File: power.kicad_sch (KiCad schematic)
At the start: 1 part, among them U1 STM32H753ZIT6

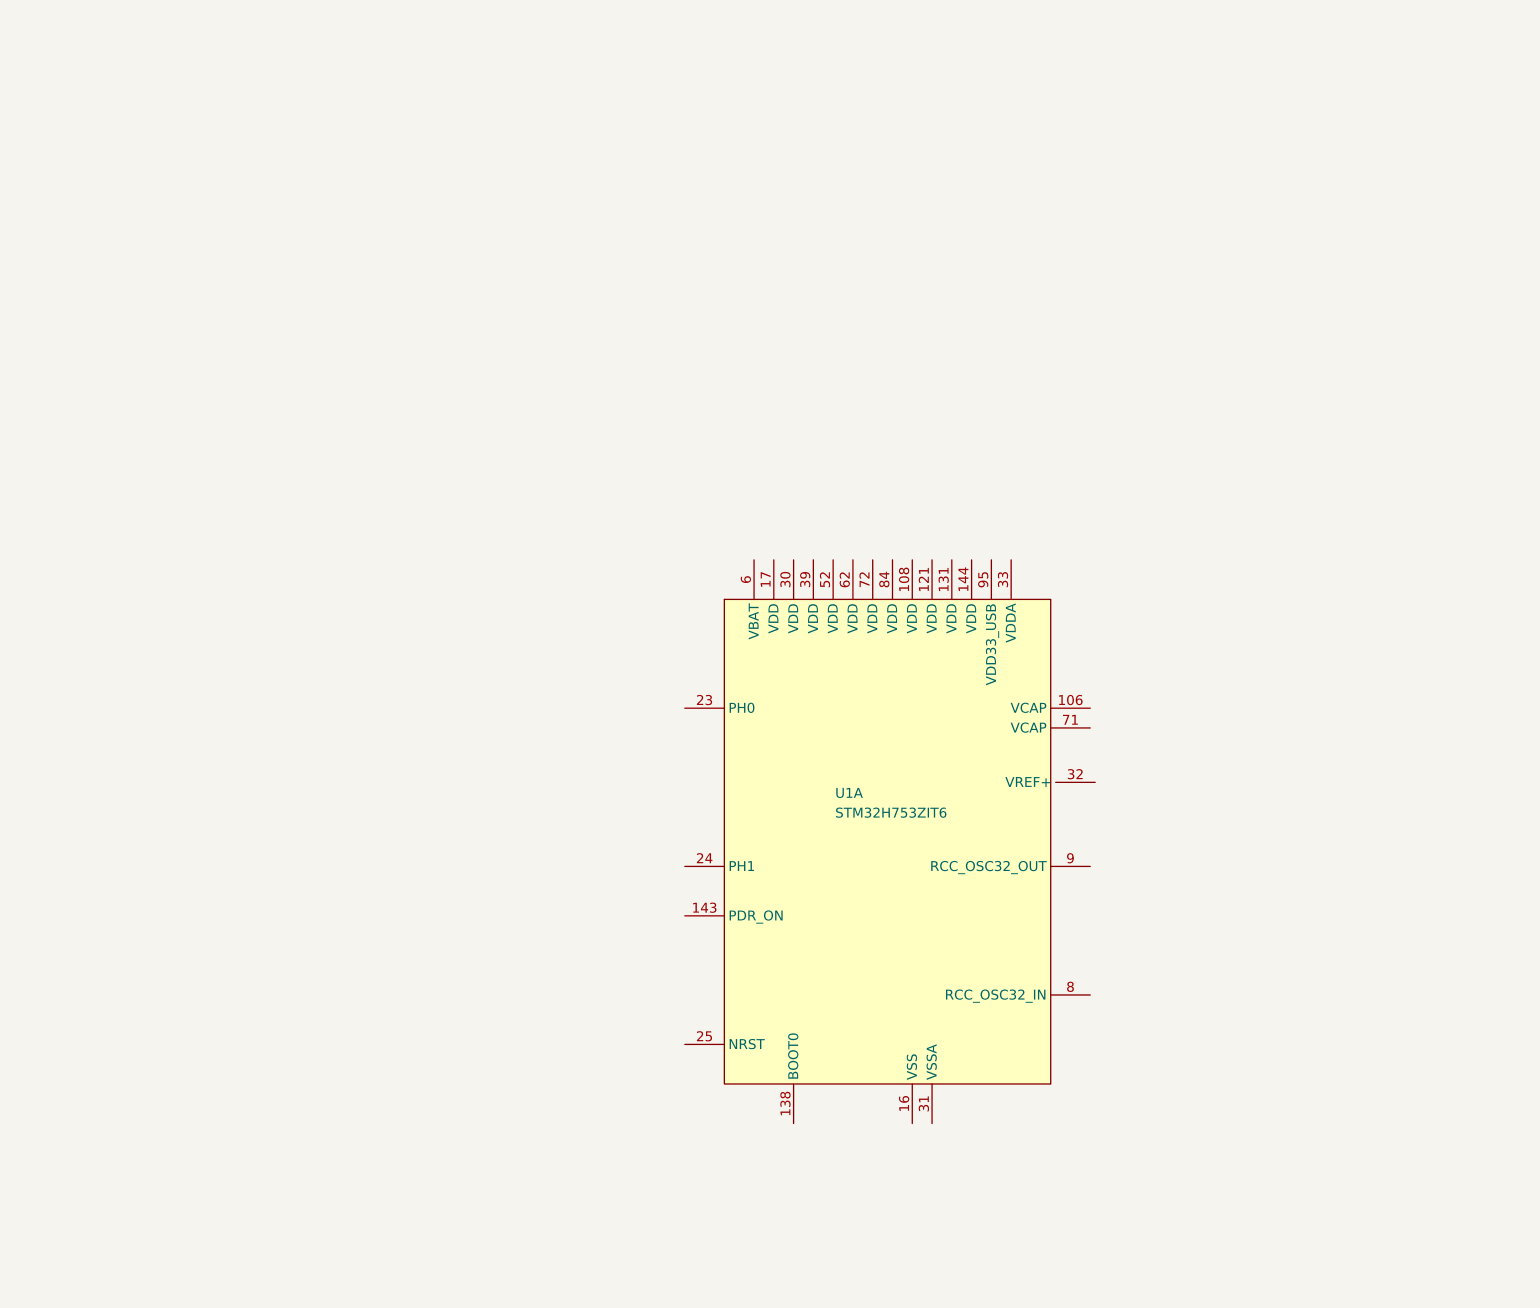
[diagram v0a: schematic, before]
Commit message: add SDIO
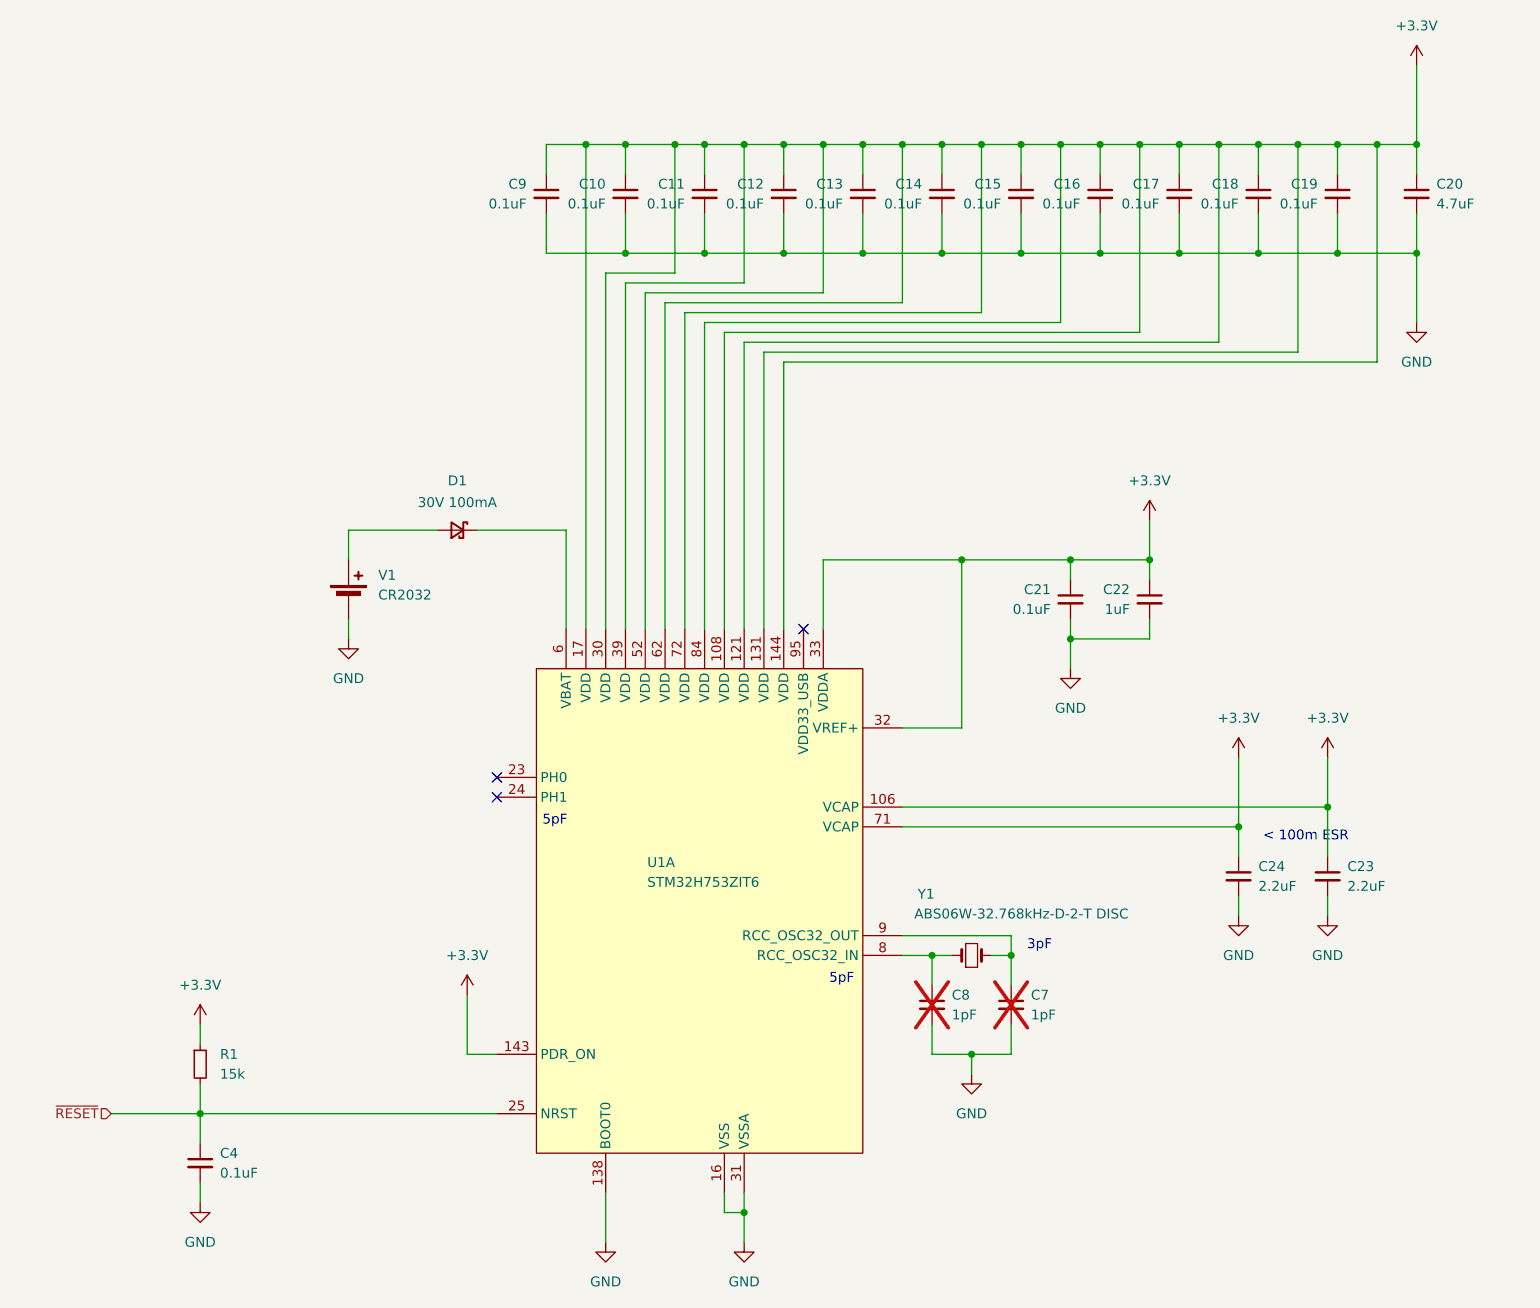
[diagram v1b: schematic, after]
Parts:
- added C10, C11, C12, C13, C14, C15, C16, C17, C18, C19, C21, C4, C9: 0.1uF, Capacitor_SMD:C_0402_1005Metric, symbol Device:C_Small
- added C20: 4.7uF, Capacitor_SMD:C_0805_2012Metric, symbol Device:C_Small
- added C22: 1uF, Capacitor_SMD:C_0402_1005Metric, symbol Device:C_Small
- added C23, C24: 2.2uF, Capacitor_SMD:C_0603_1608Metric, symbol Device:C_Small
- added C7, C8: 1pF, Capacitor_SMD:C_0402_1005Metric, symbol Device:C_Small
- added D1: 30V 100mA, Diode_SMD:D_0603_1608Metric, symbol Part-DB:CDBU0130L-HF
- added R1: 15k, Resistor_SMD:R_0402_1005Metric, symbol Device:R_Small
- added V1: CR2032, Battery:BatteryHolder_Keystone_1060_1x2032, symbol Part-DB:1060
- added Y1: ABS06W-32.768kHz-D-2-T DISC, symbol Part-DB:ABS06W-32.768kHz-D-2-T DISC
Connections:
- net +3.3V: now reaches U1.106 (VCAP)
- net +3.3V: now also U1.108 (VDD), U1.121 (VDD), U1.131 (VDD), U1.143 (PDR_ON), U1.144 (VDD), U1.17 (VDD), U1.30 (VDD), U1.32 (VREF+), U1.33 (VDDA), U1.39 (VDD), U1.52 (VDD), U1.62 (VDD), U1.71 (VCAP), U1.72 (VDD), U1.84 (VDD), C10.1, C11.1, C12.1, C13.1, C14.1, C15.1, C16.1, C17.1, C18.1, C19.1, C20.1, C21.1, C22.1, C23.1, C24.1, C9.1, R1.1
- net GND: now reaches U1.138 (BOOT0)
- net GND: now also U1.16 (VSS), U1.31 (VSSA), C10.2, C11.2, C12.2, C13.2, C14.2, C15.2, C16.2, C17.2, C18.2, C19.2, C20.2, C21.2, C22.2, C23.2, C24.2, C4.2, C7.2, C8.2, C9.2, V1.2 (-)
- net ~{RESET}: now reaches U1.25 (NRST)
- net ~{RESET}: now also C4.1, R1.2
- net at U1.6 (VBAT): now also D1.1 (K)
- net at U1.8 (RCC_OSC32_IN): now also C8.1, Y1.1
- net at U1.9 (RCC_OSC32_OUT): now also C7.1, Y1.2
- new net: D1.2 (A), V1.1 (+)
- no-connect marks 0 -> 3
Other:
- note added: "3pF"
- note added: "5pF"
- note added: "< 100m ESR"
- moved on the sheet: U1A

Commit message: checkpoint
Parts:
- Y1: footprint (none) -> Crystal:Crystal_SMD_2012-2Pin_2.0x1.2mm
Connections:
- net +3.3V: no longer C23.1, C24.1, U1.106 (VCAP), U1.71 (VCAP)
- net GND: now also U1.107 (VSS), U1.120 (VSS), U1.130 (VSS), U1.38 (VSS), U1.51 (VSS), U1.61 (VSS), U1.83 (VSS), U1.94 (VSS)
- new net: C23.1, U1.106 (VCAP)
- new net: C24.1, U1.71 (VCAP)

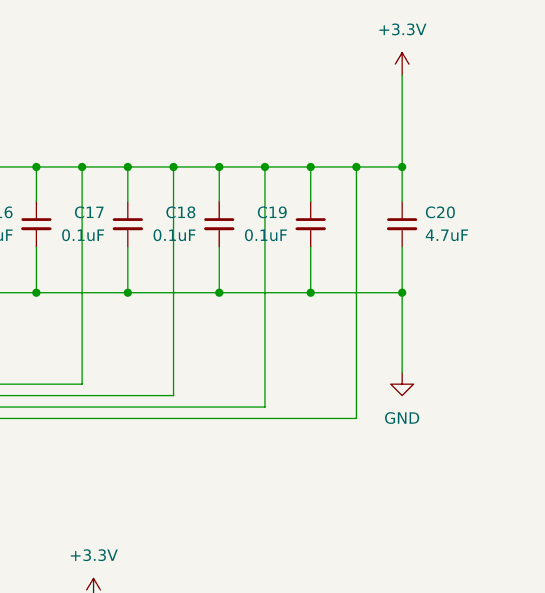
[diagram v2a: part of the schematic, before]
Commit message: VDD zone
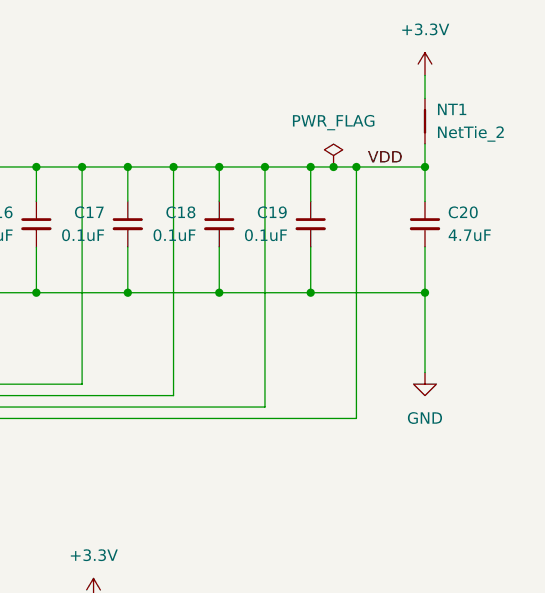
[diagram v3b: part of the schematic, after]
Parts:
- added NT1: NetTie_2, NetTie:NetTie-2_SMD_Pad0.5mm, symbol Device:NetTie_2
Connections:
- net +3.3V: now also NT1.2; no longer C10.1, C11.1, C12.1, C13.1, C14.1, C15.1, C16.1, C17.1, C18.1, C19.1, C20.1, C9.1, U1.108 (VDD), U1.121 (VDD), U1.131 (VDD), U1.144 (VDD), U1.17 (VDD), U1.30 (VDD), U1.39 (VDD), U1.52 (VDD), U1.62 (VDD), U1.72 (VDD), U1.84 (VDD)
- new net VDD: C10.1, C11.1, C12.1, C13.1, C14.1, C15.1, C16.1, C17.1, C18.1, C19.1, C20.1, C9.1, NT1.1, U1.108 (VDD), U1.121 (VDD), U1.131 (VDD), U1.144 (VDD), U1.17 (VDD), U1.30 (VDD), U1.39 (VDD), U1.52 (VDD), U1.62 (VDD), U1.72 (VDD), U1.84 (VDD)
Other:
- moved on the sheet: C20
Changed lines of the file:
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@@
 	)
 	(junction
-		(at 213.36 45.72)
+		(at 215.9 45.72)
 		(diameter 0)
 		(color 0 0 0 0)
@@
 	)
 	(junction
-		(at 213.36 31.75)
+		(at 215.9 31.75)
 		(diameter 0)
 		(color 0 0 0 0)
@@
 		(color 0 0 0 0)
 	)
+	(junction
+		(at 205.74 31.75)
+		(diameter 0)
+		(color 0 0 0 0)
+	)
 	(no_connect
 		(at 95.25 115.57)
@@
 	(wire
 		(pts
-			(xy 213.36 31.75) (xy 208.28 31.75)
+			(xy 215.9 31.75) (xy 208.28 31.75)
 		)
 		(stroke
@@
 	(wire
 		(pts
+			(xy 205.74 31.75) (xy 203.2 31.75)
+		)
+		(stroke
+			(width 0)
+			(type default)
+		)
+	)
+	(wire
+		(pts
 			(xy 168.91 85.09) (xy 154.94 85.09)
 		)
@@
 	(wire
 		(pts
+			(xy 215.9 29.21) (xy 215.9 31.75)
+		)
+		(stroke
+			(width 0)
+			(type default)
+		)
+	)
+	(wire
+		(pts
 			(xy 168.91 92.71) (xy 168.91 95.25)
 		)
@@
 	(wire
 		(pts
-			(xy 208.28 31.75) (xy 203.2 31.75)
+			(xy 208.28 31.75) (xy 205.74 31.75)
 		)
 		(stroke
@@
 	(wire
 		(pts
-			(xy 213.36 40.64) (xy 213.36 45.72)
+			(xy 215.9 40.64) (xy 215.9 45.72)
 		)
 		(stroke
@@
 	(wire
 		(pts
-			(xy 213.36 21.59) (xy 213.36 31.75)
+			(xy 215.9 21.59) (xy 215.9 24.13)
 		)
 		(stroke
@@
 	(wire
 		(pts
-			(xy 213.36 45.72) (xy 213.36 54.61)
+			(xy 215.9 45.72) (xy 215.9 54.61)
 		)
 		(stroke
@@
 	(wire
 		(pts
-			(xy 213.36 31.75) (xy 213.36 35.56)
+			(xy 215.9 31.75) (xy 215.9 35.56)
 		)
 		(stroke
@@
 	(wire
 		(pts
-			(xy 213.36 45.72) (xy 203.2 45.72)
+			(xy 215.9 45.72) (xy 203.2 45.72)
 		)
 		(stroke
@@
 		)
 	)
+	(label "VDD"
+		(at 209.55 31.75 0)
+		(fields_autoplaced yes)
+		(effects
+			(font
+				(size 1.27 1.27)
+			)
+			(justify left bottom)
+		)
+	)
 	(hierarchical_label "~{RESET}"
 		(shape output)
@@
 	)
 	(symbol
+		(lib_id "power:PWR_FLAG")
+		(at 205.74 31.75 0)
+		(unit 1)
+		(exclude_from_sim no)
+		(in_bom yes)
+		(on_board yes)
+		(dnp no)
+		(fields_autoplaced yes)
+		(property "Reference" "#FLG09"
+			(at 205.74 29.845 0)
+			(effects
+				(font
+					(size 1.27 1.27)
+				)
+				(hide yes)
+			)
+		)
+		(property "Value" "PWR_FLAG"
+			(at 205.74 26.67 0)
+			(effects
+				(font
+					(size 1.27 1.27)
+				)
+			)
+		)
+		(property "Footprint" ""
+			(at 205.74 31.75 0)
+			(effects
+				(font
+					(size 1.27 1.27)
+				)
+				(hide yes)
+			)
+		)
+		(property "Datasheet" "~"
+			(at 205.74 31.75 0)
+			(effects
+				(font
+					(size 1.27 1.27)
+				)
+				(hide yes)
+			)
+		)
+		(property "Description" "Special symbol for telling ERC where power comes from"
+			(at 205.74 31.75 0)
+			(effects
+				(font
+					(size 1.27 1.27)
+				)
+				(hide yes)
+			)
+		)
+		(pin "1"
+		)
+		(instances
+			(project ""
+				(path "/114c4e64-0fac-420a-8fa7-2afba1510345/fbfd422a-57f1-4eb0-a9e8-3ef120646a70"
+					(reference "#FLG09")
+					(unit 1)
+				)
+			)
+		)
+	)
+	(symbol
 		(lib_id "Device:C_Small")
 		(at 182.88 38.1 0)
@@
 	(symbol
 		(lib_id "Device:C_Small")
-		(at 213.36 38.1 0)
+		(at 215.9 38.1 0)
 		(unit 1)
 		(exclude_from_sim no)
@@
 		(fields_autoplaced yes)
 		(property "Reference" "C20"
-			(at 215.9 36.8362 0)
+			(at 218.44 36.8362 0)
 			(effects
 				(font
@@
 		)
 		(property "Value" "4.7uF"
-			(at 215.9 39.3762 0)
+			(at 218.44 39.3762 0)
 			(effects
 				(font
@@
 		)
 		(property "Footprint" "Capacitor_SMD:C_0805_2012Metric"
-			(at 213.36 38.1 0)
+			(at 215.9 38.1 0)
 			(effects
 				(font
@@
 		)
 		(property "Datasheet" "~"
-			(at 213.36 38.1 0)
+			(at 215.9 38.1 0)
 			(effects
 				(font
@@
 		)
 		(property "Description" "Unpolarized capacitor, small symbol"
-			(at 213.36 38.1 0)
+			(at 215.9 38.1 0)
 			(effects
 				(font
@@
 	(symbol
 		(lib_id "power:+3.3V")
-		(at 213.36 21.59 0)
+		(at 215.9 21.59 0)
 		(unit 1)
 		(exclude_from_sim no)
@@
 		(fields_autoplaced yes)
 		(property "Reference" "#PWR018"
-			(at 213.36 25.4 0)
+			(at 215.9 25.4 0)
 			(effects
 				(font
@@
 		)
 		(property "Value" "+3.3V"
-			(at 213.36 16.51 0)
+			(at 215.9 16.51 0)
 			(effects
 				(font
@@
 		)
 		(property "Footprint" ""
-			(at 213.36 21.59 0)
+			(at 215.9 21.59 0)
 			(effects
 				(font
@@
 		)
 		(property "Datasheet" ""
-			(at 213.36 21.59 0)
+			(at 215.9 21.59 0)
 			(effects
 				(font
@@
 		)
 		(property "Description" "Power symbol creates a global label with name \"+3.3V\""
-			(at 213.36 21.59 0)
+			(at 215.9 21.59 0)
 			(effects
 				(font
@@
 	(symbol
 		(lib_id "power:GND")
-		(at 213.36 54.61 0)
+		(at 215.9 54.61 0)
 		(unit 1)
 		(exclude_from_sim no)
@@
 		(fields_autoplaced yes)
 		(property "Reference" "#PWR019"
-			(at 213.36 60.96 0)
+			(at 215.9 60.96 0)
 			(effects
 				(font
@@
 		)
 		(property "Value" "GND"
-			(at 213.36 59.69 0)
+			(at 215.9 59.69 0)
 			(effects
 				(font
@@
 		)
 		(property "Footprint" ""
-			(at 213.36 54.61 0)
+			(at 215.9 54.61 0)
 			(effects
 				(font
@@
 		)
 		(property "Datasheet" ""
-			(at 213.36 54.61 0)
+			(at 215.9 54.61 0)
 			(effects
 				(font
@@
 		)
 		(property "Description" "Power symbol creates a global label with name \"GND\" , ground"
-			(at 213.36 54.61 0)
+			(at 215.9 54.61 0)
 			(effects
 				(font
@@
 					(unit 1)
 				)
+			)
+		)
+	)
+	(symbol
+		(lib_id "Device:NetTie_2")
+		(at 215.9 26.67 90)
+		(unit 1)
+		(exclude_from_sim no)
+		(in_bom no)
+		(on_board yes)
+		(dnp no)
+		(fields_autoplaced yes)
+		(property "Reference" "NT1"
+			(at 217.17 25.3999 90)
+			(effects
+				(font
+					(size 1.27 1.27)
+				)
+				(justify right)
+			)
+		)
+		(property "Value" "NetTie_2"
+			(at 217.17 27.9399 90)
+			(effects
+				(font
+					(size 1.27 1.27)
+				)
+				(justify right)
+			)
+		)
+		(property "Footprint" "NetTie:NetTie-2_SMD_Pad0.5mm"
+			(at 215.9 26.67 0)
+			(effects
+				(font
+					(size 1.27 1.27)
+				)
+				(hide yes)
+			)
+		)
+		(property "Datasheet" "~"
+			(at 215.9 26.67 0)
+			(effects
+				(font
+					(size 1.27 1.27)
+				)
+				(hide yes)
+			)
+		)
+		(property "Description" "Net tie, 2 pins"
+			(at 215.9 26.67 0)
+			(effects
+				(font
+					(size 1.27 1.27)
+				)
+				(hide yes)
+			)
+		)
+		(pin "2"
+		)
+		(pin "1"
+		)
+		(instances
+			(project ""
+				(path "/114c4e64-0fac-420a-8fa7-2afba1510345/fbfd422a-57f1-4eb0-a9e8-3ef120646a70"
+					(reference "NT1")
+					(unit 1)
+				)

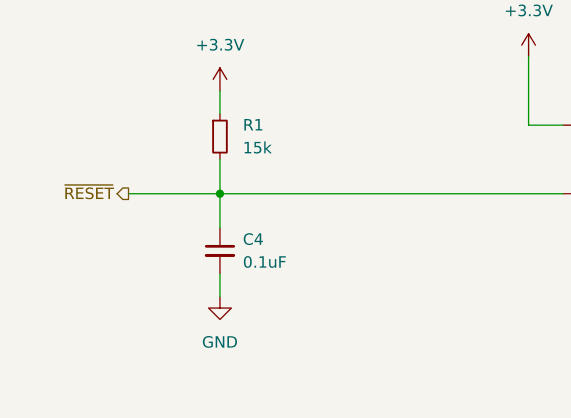
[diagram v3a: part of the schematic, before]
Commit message: add reset button
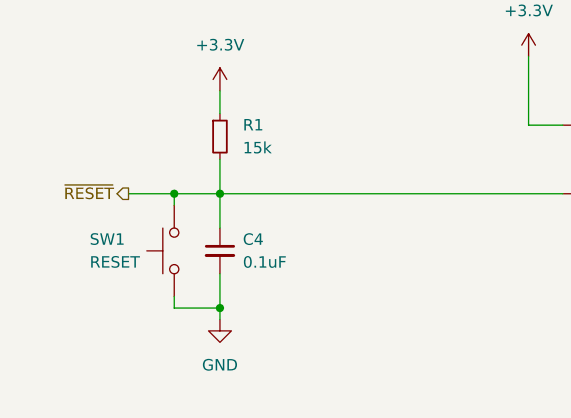
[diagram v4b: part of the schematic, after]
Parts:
- added SW1: RESET, Button_Switch_SMD:SW_SPST_CK_RS282G05A3, symbol Switch:SW_Push
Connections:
- net GND: now also SW1.2
- net ~{RESET}: now also SW1.1
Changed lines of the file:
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@@
 	(paper "A4")
 	(junction
+		(at 57.15 168.91)
+		(diameter 0)
+		(color 0 0 0 0)
+	)
+	(junction
 		(at 132.08 45.72)
 		(diameter 0)
@@
 	(junction
 		(at 193.04 31.75)
+		(diameter 0)
+		(color 0 0 0 0)
+	)
+	(junction
+		(at 52.07 156.21)
 		(diameter 0)
 		(color 0 0 0 0)
@@
 	(wire
 		(pts
-			(xy 57.15 165.1) (xy 57.15 167.64)
+			(xy 57.15 165.1) (xy 57.15 168.91)
 		)
 		(stroke
@@
 	(wire
 		(pts
-			(xy 46.99 156.21) (xy 57.15 156.21)
+			(xy 46.99 156.21) (xy 52.07 156.21)
 		)
 		(stroke
@@
 	(wire
 		(pts
+			(xy 52.07 167.64) (xy 52.07 168.91)
+		)
+		(stroke
+			(width 0)
+			(type default)
+		)
+	)
+	(wire
+		(pts
 			(xy 168.91 85.09) (xy 154.94 85.09)
 		)
@@
 	(wire
 		(pts
+			(xy 52.07 156.21) (xy 52.07 157.48)
+		)
+		(stroke
+			(width 0)
+			(type default)
+		)
+	)
+	(wire
+		(pts
 			(xy 154.94 106.68) (xy 154.94 85.09)
 		)
@@
 	(wire
 		(pts
+			(xy 52.07 156.21) (xy 57.15 156.21)
+		)
+		(stroke
+			(width 0)
+			(type default)
+		)
+	)
+	(wire
+		(pts
 			(xy 147.32 135.89) (xy 151.13 135.89)
 		)
@@
 	(wire
 		(pts
+			(xy 52.07 168.91) (xy 57.15 168.91)
+		)
+		(stroke
+			(width 0)
+			(type default)
+		)
+	)
+	(wire
+		(pts
 			(xy 104.14 81.28) (xy 104.14 93.98)
 		)
@@
 		(pts
 			(xy 121.92 54.61) (xy 121.92 93.98)
+		)
+		(stroke
+			(width 0)
+			(type default)
+		)
+	)
+	(wire
+		(pts
+			(xy 57.15 168.91) (xy 57.15 170.18)
 		)
 		(stroke
@@
 			)
 			(justify right)
+		)
+	)
+	(symbol
+		(lib_id "Switch:SW_Push")
+		(at 52.07 162.56 90)
+		(mirror x)
+		(unit 1)
+		(exclude_from_sim no)
+		(in_bom yes)
+		(on_board yes)
+		(dnp no)
+		(property "Reference" "SW1"
+			(at 42.672 161.29 90)
+			(effects
+				(font
+					(size 1.27 1.27)
+				)
+				(justify right)
+			)
+		)
+		(property "Value" "RESET"
+			(at 42.672 163.83 90)
+			(effects
+				(font
+					(size 1.27 1.27)
+				)
+				(justify right)
+			)
+		)
+		(property "Footprint" "Button_Switch_SMD:SW_SPST_CK_RS282G05A3"
+			(at 46.99 162.56 0)
+			(effects
+				(font
+					(size 1.27 1.27)
+				)
+				(hide yes)
+			)
+		)
+		(property "Datasheet" "~"
+			(at 46.99 162.56 0)
+			(effects
+				(font
+					(size 1.27 1.27)
+				)
+				(hide yes)
+			)
+		)
+		(property "Description" "Push button switch, generic, two pins"
+			(at 52.07 162.56 0)
+			(effects
+				(font
+					(size 1.27 1.27)
+				)
+				(hide yes)
+			)
+		)
+		(pin "2"
+		)
+		(pin "1"
+		)
+		(instances
+			(project "stm32simh"
+				(path "/114c4e64-0fac-420a-8fa7-2afba1510345/fbfd422a-57f1-4eb0-a9e8-3ef120646a70"
+					(reference "SW1")
+					(unit 1)
+				)
+			)
 		)
 	)
@@
 	(symbol
 		(lib_id "power:GND")
-		(at 57.15 167.64 0)
+		(at 57.15 170.18 0)
 		(unit 1)
 		(exclude_from_sim no)
@@
 		(fields_autoplaced yes)
 		(property "Reference" "#PWR011"
-			(at 57.15 173.99 0)
+			(at 57.15 176.53 0)
 			(effects
 				(font
@@
 		)
 		(property "Value" "GND"
-			(at 57.15 172.72 0)
+			(at 57.15 175.26 0)
 			(effects
 				(font
@@
 		)
 		(property "Footprint" ""
-			(at 57.15 167.64 0)
+			(at 57.15 170.18 0)
 			(effects
 				(font
@@
 		)
 		(property "Datasheet" ""
-			(at 57.15 167.64 0)
+			(at 57.15 170.18 0)
 			(effects
 				(font
@@
 		)
 		(property "Description" "Power symbol creates a global label with name \"GND\" , ground"
-			(at 57.15 167.64 0)
-			(effects
-				(font
+			(at 57.15 170.18 0)
+			(effects
+				(font
